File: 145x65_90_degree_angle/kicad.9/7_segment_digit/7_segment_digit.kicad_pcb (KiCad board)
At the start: 2 copper layers, 65 x 145 mm, 14 parts, among them X1 PLS-10

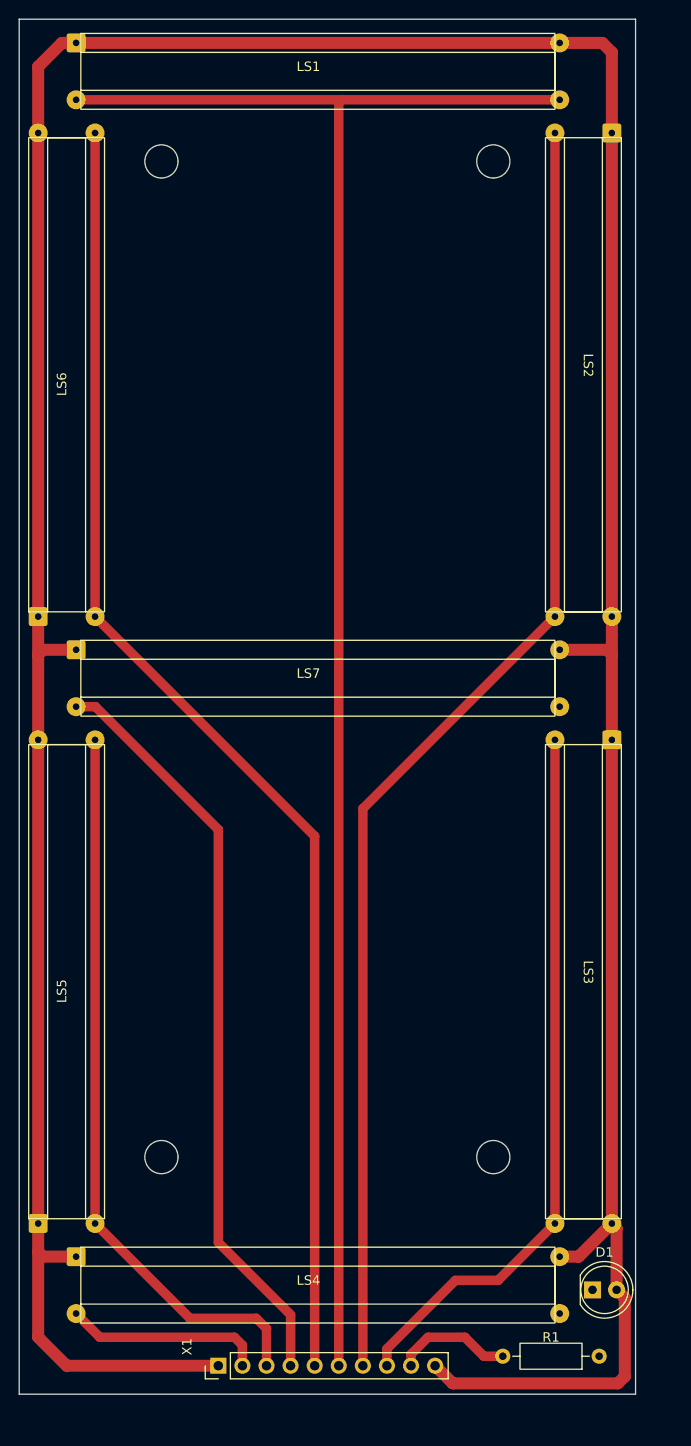
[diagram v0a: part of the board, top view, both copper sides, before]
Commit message: Добавил символ и посадочную площадку СИД SMD 5050. Обновил схему и ПП.
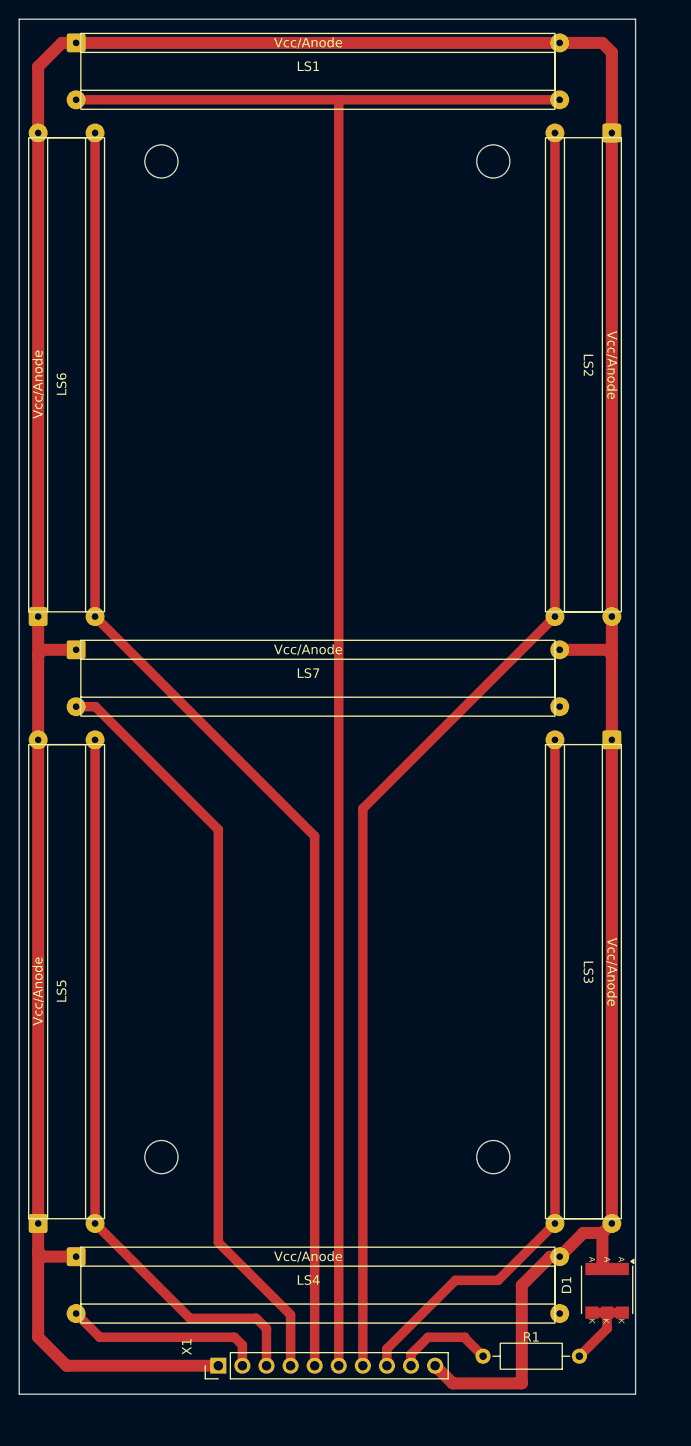
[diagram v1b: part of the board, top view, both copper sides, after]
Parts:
- D1: value LED -> ~; footprint LED_THT:LED_D5.0mm -> led_strip:LED_SMD_5050_6
- moved R1 2.08 mm to (113.6, 169.5)
- moved D1 1.54 mm to (116.5, 162.5), turned to -90 degrees
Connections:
- D1 pad 1: /1 -> VCC
- D1 pad 2: VCC -> /1
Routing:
- net /1: track 0.00 -> 9.01 mm
- net VCC: track 398.5 -> 393.5 mm
- net /SEG_DP: track 12.5 -> 10.4 mm
